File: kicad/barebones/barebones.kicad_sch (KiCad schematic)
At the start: 12 parts, among them J101 PAL-1 Expansion Connector, J102 G27, J103 WE, SW101 PICO RESET, SW102 SW_DIP_x08, U101 74LS01, U102 74LS145, U104 Pico

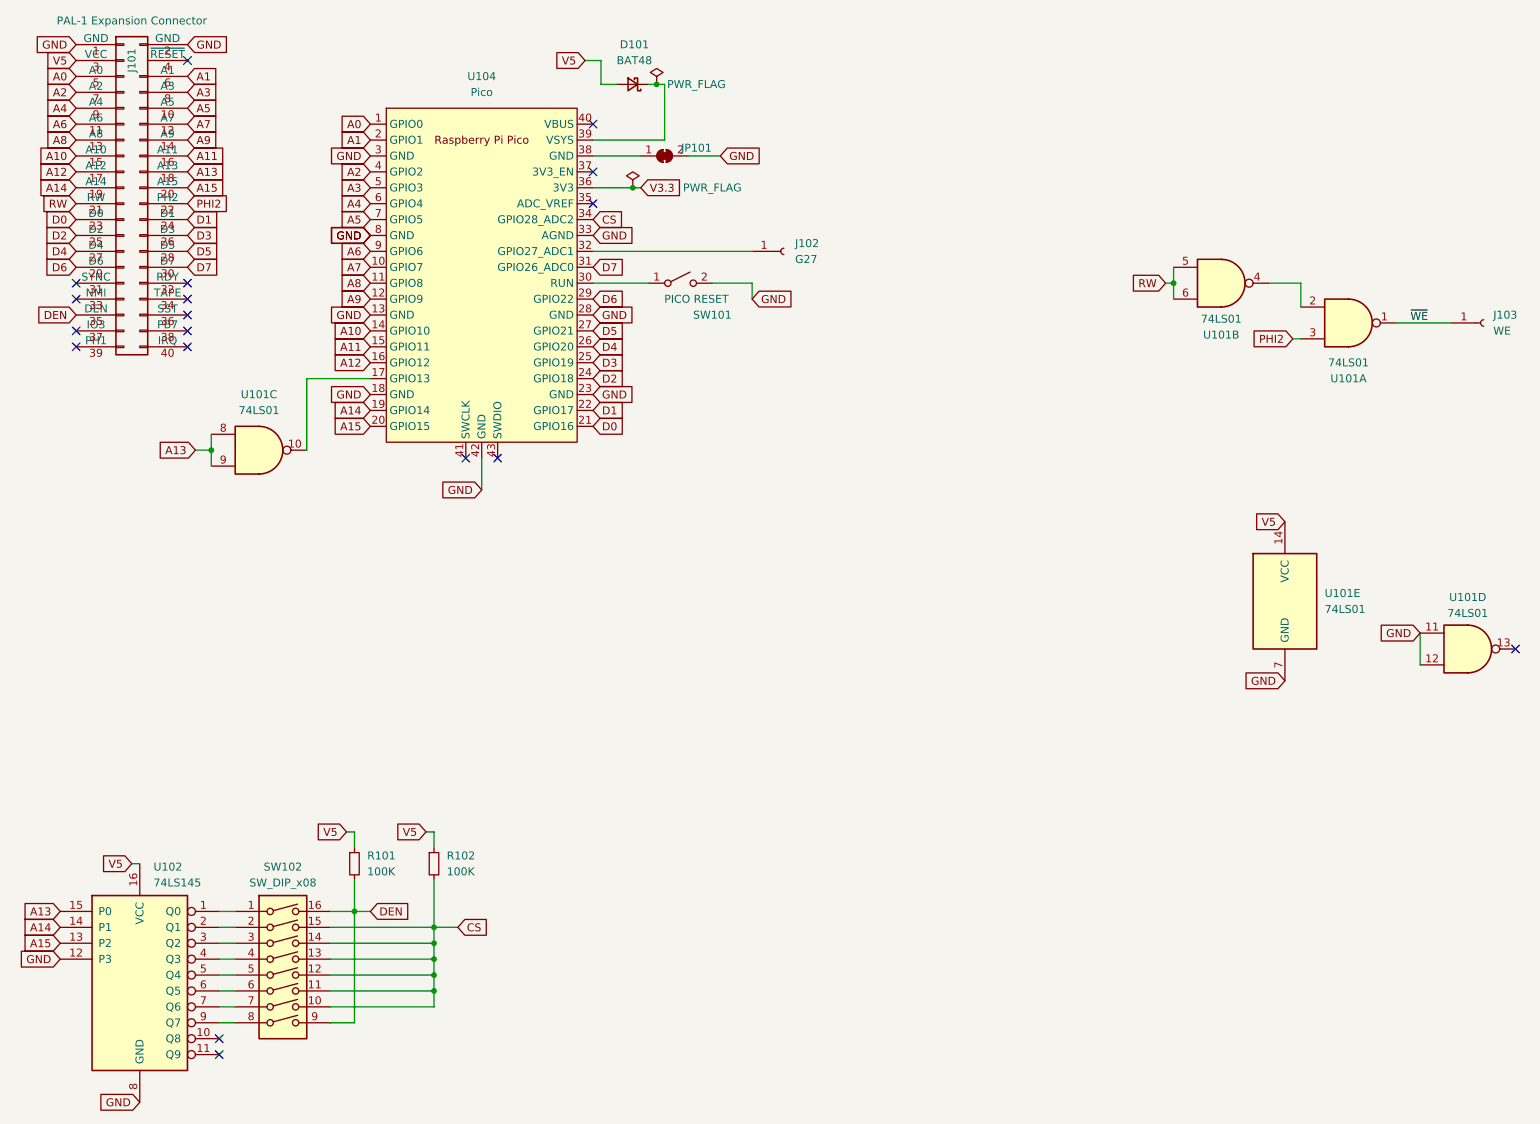
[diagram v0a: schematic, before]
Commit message: Updated code so that CS works correctly, started next PCB version
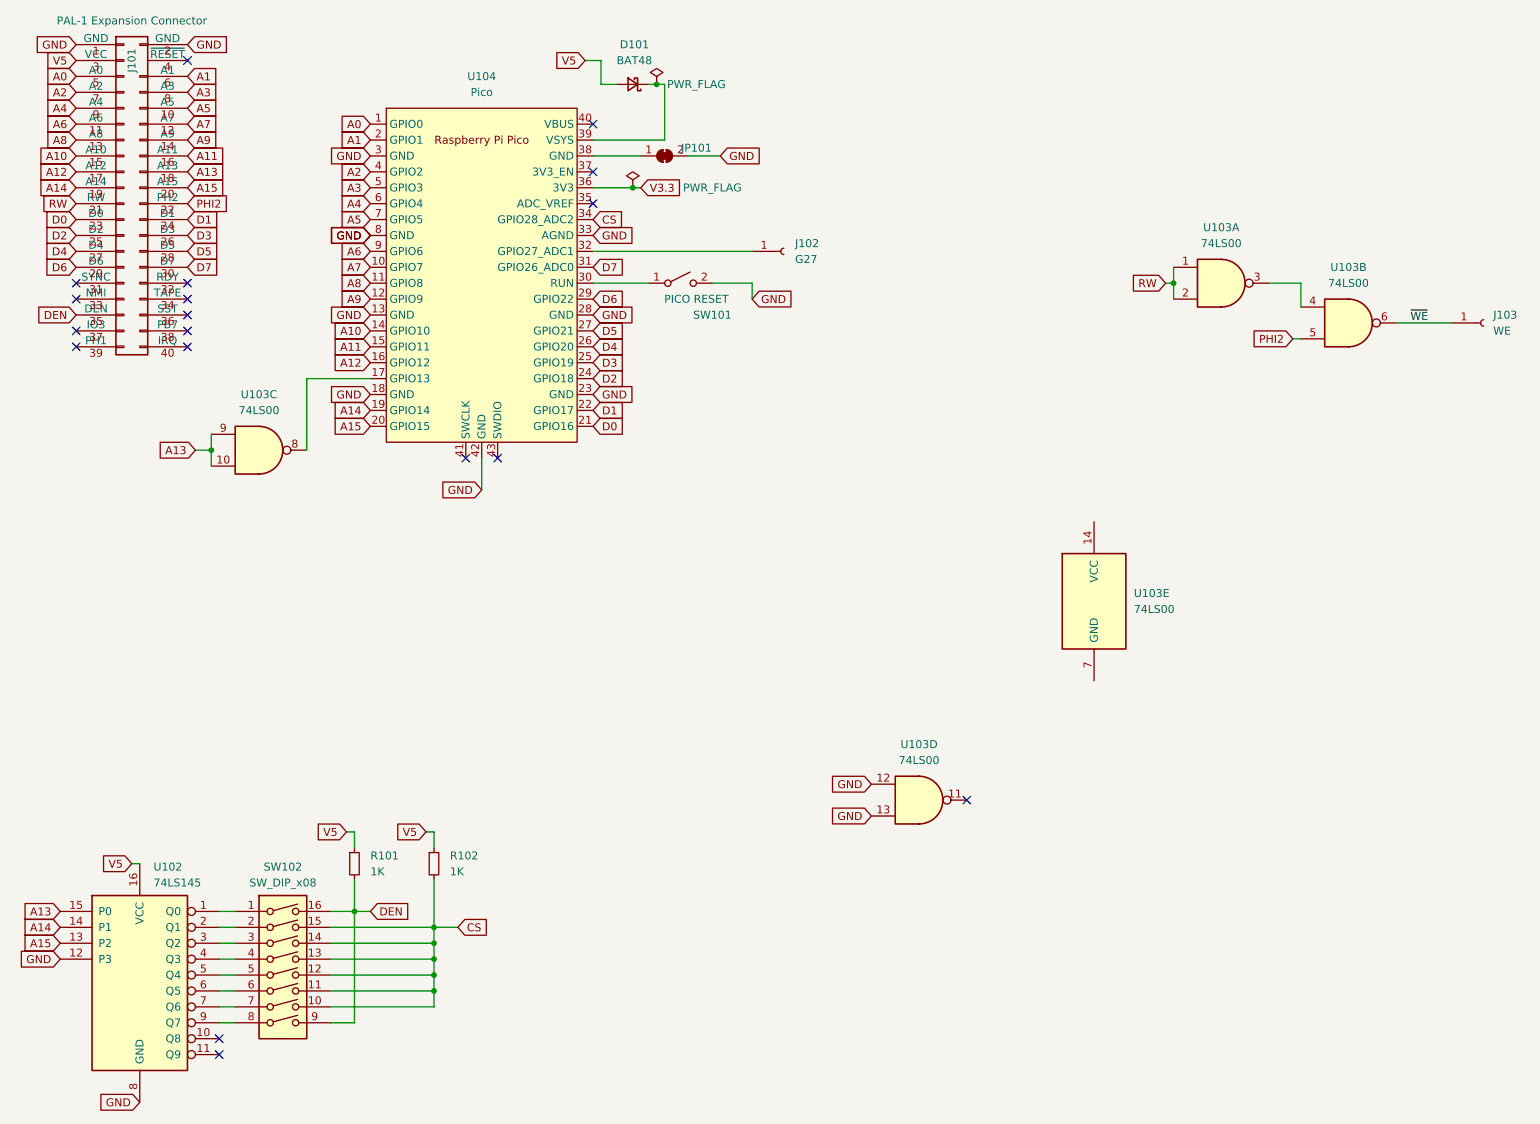
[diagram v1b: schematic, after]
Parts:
- removed U101: 74LS01, Package_DIP:DIP-14_W7.62mm_Socket_LongPads, symbol 74xx:74LS01
- added U103: 74LS00, Package_DIP:DIP-14_W7.62mm_Socket_LongPads, symbol 74xx:74LS00
- R101, R102: value 100K -> 1K
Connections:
- net A13: now also U103.10, U103.9
- net GND: now also U103.12, U103.13
- net PHI2: now also U103.5
- net RW: now also U103.1, U103.2
- net ~{WE}: now also U103.6
- net at U104.17 (GPIO13): now also U103.8
- new net: U103.3, U103.4

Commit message: RAM working and updating. PHI2 respected.
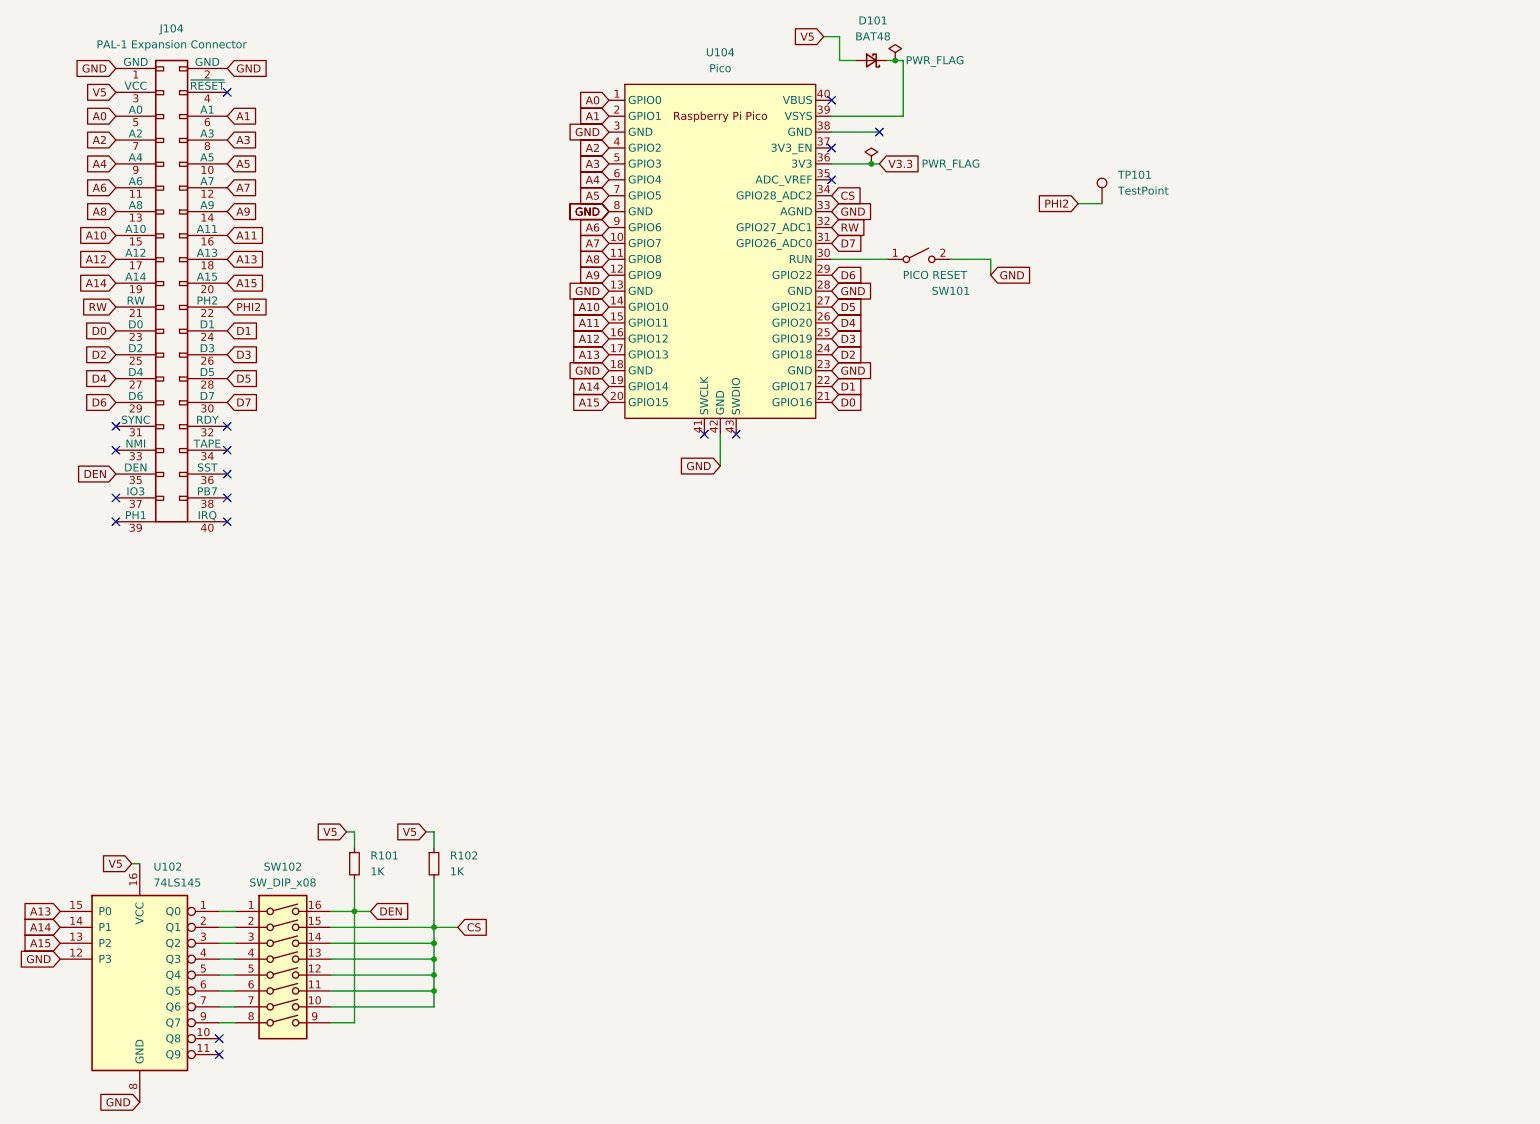
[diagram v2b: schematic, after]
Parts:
- removed J101: PAL-1 Expansion Connector, Connector_PinHeader_2.54mm:PinHeader_2x20_P2.54mm_Horizontal, symbol pal1:Expansion_Connector
- removed J102: G27, Connector_PinHeader_2.54mm:PinHeader_1x01_P2.54mm_Vertical, symbol Connector:Conn_01x01_Socket
- removed J103: WE, Connector_PinHeader_2.54mm:PinHeader_1x01_P2.54mm_Vertical, symbol Connector:Conn_01x01_Socket
- removed JP101: SolderJumper_2_Bridged, Jumper:SolderJumper-2_P1.3mm_Bridged2Bar_RoundedPad1.0x1.5mm, symbol Jumper:SolderJumper_2_Bridged
- removed U103: 74LS00, Package_DIP:DIP-14_W7.62mm_Socket_LongPads, symbol 74xx:74LS00
- added J104: PAL-1 Expansion Connector, Connector_PinHeader_2.54mm:PinHeader_2x20_P2.54mm_Vertical, symbol pal1:Expansion_Connector
- added TP101: TestPoint, TestPoint:TestPoint_Pad_2.5x2.5mm, symbol Connector:TestPoint
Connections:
- net A0: now also J104.5 (A0)
- net A1: now also J104.6 (A1)
- net A10: now also J104.15 (A10)
- net A11: now also J104.16 (A11)
- net A12: now also J104.17 (A12)
- net A13: now also U104.17 (GPIO13), J104.18 (A13)
- net A14: now also J104.19 (A14)
- net A15: now also J104.20 (A15)
- net A2: now also J104.7 (A2)
- net A3: now also J104.8 (A3)
- net A4: now also J104.9 (A4)
- net A5: now also J104.10 (A5)
- net A6: now also J104.11 (A6)
- net A7: now also J104.12 (A7)
- net A8: now also J104.13 (A8)
- net A9: now also J104.14 (A9)
- net D0: now also J104.23 (D0)
- net D1: now also J104.24 (D1)
- net D2: now also J104.25 (D2)
- net D3: now also J104.26 (D3)
- net D4: now also J104.27 (D4)
- net D5: now also J104.28 (D5)
- net D6: now also J104.29 (D6)
- net D7: now also J104.30 (D7)
- net DEN: now also J104.35 (DEN)
- net GND: now also J104.1 (GND), J104.2 (GND)
- net PHI2: now also J104.22 (PH2), TP101.1
- net RW: now also U104.32 (GPIO27_ADC1), J104.21 (RW)
- net V5: now also J104.3 (VCC)
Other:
- moved on the sheet: D101, SW101, U104

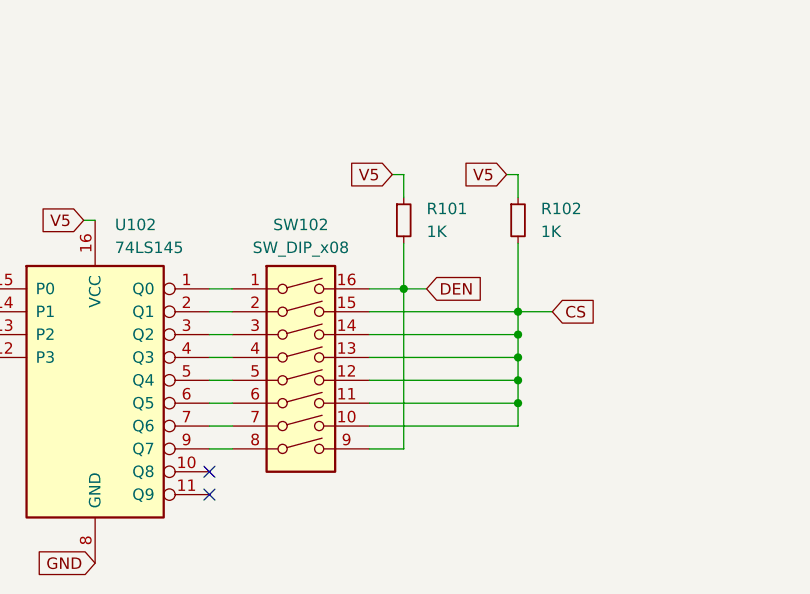
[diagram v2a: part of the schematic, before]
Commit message: Bit of PCB cleanup for removed features.
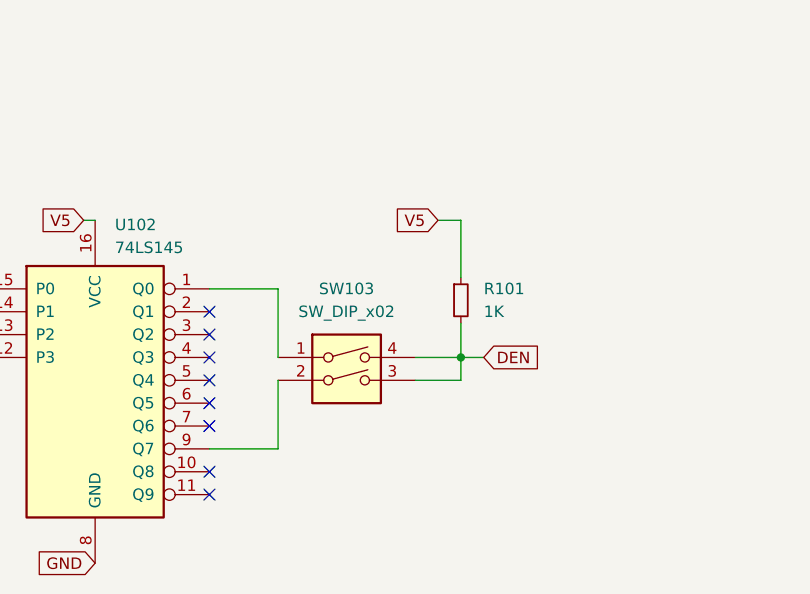
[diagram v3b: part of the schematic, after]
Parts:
- removed R102: 1K, Resistor_THT:R_Axial_DIN0204_L3.6mm_D1.6mm_P5.08mm_Horizontal, symbol Device:R_Small
- removed SW102: SW_DIP_x08, Button_Switch_THT:SW_DIP_SPSTx08_Slide_6.7x21.88mm_W7.62mm_P2.54mm_LowProfile, symbol Switch:SW_DIP_x08
- added SW103: SW_DIP_x02, Button_Switch_THT:SW_DIP_SPSTx02_Slide_9.78x7.26mm_W7.62mm_P2.54mm, symbol Switch:SW_DIP_x02
- R101: footprint Resistor_THT:R_Axial_DIN0204_L3.6mm_D1.6mm_P5.08mm_Horizontal -> Resistor_THT:R_Axial_DIN0207_L6.3mm_D2.5mm_P10.16mm_Horizontal
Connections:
- net DEN: now also SW103.3, SW103.4
- net at U102.1 (Q0): now also SW103.1
- net at U102.9 (Q7): now also SW103.2
- no-connect marks 18 -> 24
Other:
- moved on the sheet: R101
